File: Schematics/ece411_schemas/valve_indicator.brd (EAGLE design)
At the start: 85.1 x 53.6 mm, 66 parts, among them IC1 STM32F042K6T6, T1 2N2222, T2 2N2222, T3 2N2222, T4 2N2222, U1 DIODES_INC._AZ34063UMTR-G1DIO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, U2 DIODES_INC._AZ34063UMTR-G1DIO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

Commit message: added bypass caps, updated bom
needed to add 10uF ceramic in parallel with 100uF electro caps to decrease resistance to ground
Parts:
- added C0_H, C0_L: 10uF, rcl:C1206
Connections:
- net GND: now also C0_H.2, C0_L.2
- net N$1: now also C0_H.1, C0_L.1
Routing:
- net N$1: track 56.5 -> 65.0 mm
- net N$21: track 49.5 -> 51.5 mm
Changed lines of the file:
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@@
 <attribute name="MOUSER_PART_NUMBER" value="621-AZ34063UMTR-G1" x="-13.335" y="38.1" size="1.778" layer="27" rot="R180" display="off"/>
 <attribute name="MPN" value="AZ34063UMTR-G1" x="-13.335" y="38.1" size="1.778" layer="27" rot="R180" display="off"/>
-<attribute name="NAME" x="34.995" y="31.515" size="1" layer="25" rot="R180"/>
+<attribute name="NAME" x="35.63" y="37.865" size="0.8128" layer="25" rot="R180"/>
 <attribute name="NOMINAL_SUPPLY_CURRENT" value="4mA" x="-13.335" y="38.1" size="1.778" layer="27" rot="R180" display="off"/>
 <attribute name="NUMBER_OF_OUTPUTS" value="1" x="-13.335" y="38.1" size="1.778" layer="27" rot="R180" display="off"/>
@@
 <attribute name="MOUSER_PART_NUMBER" value="621-AZ34063UMTR-G1" x="51.435" y="22.86" size="1.778" layer="27" display="off"/>
 <attribute name="MPN" value="AZ34063UMTR-G1" x="51.435" y="22.86" size="1.778" layer="27" display="off"/>
-<attribute name="NAME" x="33.585" y="43.415" size="1" layer="25"/>
+<attribute name="NAME" x="34.22" y="43.415" size="0.8128" layer="25"/>
 <attribute name="NOMINAL_SUPPLY_CURRENT" value="4mA" x="51.435" y="22.86" size="1.778" layer="27" display="off"/>
 <attribute name="NUMBER_OF_OUTPUTS" value="1" x="51.435" y="22.86" size="1.778" layer="27" display="off"/>
@@
 <attribute name="POPULARITY" value="0" x="40.005" y="45.085" size="1.778" layer="27" rot="R180" display="off"/>
 <attribute name="SPICEPREFIX" value="C" x="40.005" y="45.085" size="1.778" layer="27" rot="R180" display="off"/>
+</element>
+<element name="C0_L" library="rcl" library_urn="urn:adsk.eagle:library:334" package="C1206" package3d_urn="urn:adsk.eagle:package:23618/2" value="10uF" x="34.29" y="45.72" smashed="yes" rot="R180">
+<attribute name="NAME" x="33.02" y="46.99" size="0.8128" layer="25"/>
+<attribute name="POPULARITY" value="24" x="34.29" y="45.72" size="1.778" layer="27" rot="R180" display="off"/>
+<attribute name="SPICEPREFIX" value="C" x="34.29" y="45.72" size="1.778" layer="27" rot="R180" display="off"/>
+</element>
+<element name="C0_H" library="rcl" library_urn="urn:adsk.eagle:library:334" package="C1206" package3d_urn="urn:adsk.eagle:package:23618/2" value="10uF" x="28.575" y="36.83" smashed="yes" rot="R90">
+<attribute name="NAME" x="29.845" y="38.1" size="0.8128" layer="25" rot="R270"/>
+<attribute name="POPULARITY" value="24" x="28.575" y="36.83" size="1.778" layer="27" rot="R90" display="off"/>
+<attribute name="SPICEPREFIX" value="C" x="28.575" y="36.83" size="1.778" layer="27" rot="R90" display="off"/>
 </element>
 </elements>
@@
 <via x="14.605" y="45.085" extent="1-16" drill="0.35"/>
 <via x="20.955" y="45.085" extent="1-16" drill="0.35"/>
-<via x="36.195" y="46.355" extent="1-16" drill="0.35"/>
+<via x="36.195" y="43.815" extent="1-16" drill="0.35"/>
 <via x="47.625" y="46.355" extent="1-16" drill="0.35"/>
 <via x="62.865" y="29.845" extent="1-16" drill="0.35"/>
@@
 <via x="3.81" y="31.75" extent="1-16" drill="0.35"/>
 <via x="3.81" y="38.735" extent="1-16" drill="0.35"/>
+<contactref element="C0_H" pad="2"/>
+<contactref element="C0_L" pad="2"/>
 </signal>
 <signal name="N$6">
@@
 <signal name="N$4">
 <contactref element="U1" pad="5"/>
-<wire x1="32.427" y1="36.195" x2="27.94" y2="36.195" width="0.3048" layer="1"/>
+<wire x1="32.427" y1="36.195" x2="30.48" y2="36.195" width="0.3048" layer="1"/>
 <contactref element="R1_L" pad="1"/>
 <contactref element="R2_L" pad="2"/>
-<wire x1="27.09" y1="37.045" x2="24.765" y2="37.045" width="0.3048" layer="1"/>
-<wire x1="27.94" y1="36.195" x2="27.09" y2="37.045" width="0.3048" layer="1"/>
+<wire x1="29.63" y1="37.045" x2="24.765" y2="37.045" width="0.3048" layer="1"/>
+<wire x1="30.48" y1="36.195" x2="29.63" y2="37.045" width="0.3048" layer="1"/>
 <wire x1="24.765" y1="37.045" x2="24.765" y2="39.155" width="0.3048" layer="1"/>
 </signal>
@@
 <wire x1="68.89" y1="36.52" x2="65.715" y2="39.695" width="0.3048" layer="1"/>
 <wire x1="56.825" y1="39.695" x2="65.715" y2="39.695" width="0.3048" layer="1"/>
-<wire x1="30.48" y1="41.91" x2="30.48" y2="43.307" width="0.3048" layer="1"/>
-<wire x1="30.48" y1="43.307" x2="34.2265" y2="47.0535" width="0.3048" layer="1"/>
+<wire x1="30.48" y1="41.91" x2="30.48" y2="45.847" width="0.3048" layer="1"/>
+<wire x1="30.48" y1="45.847" x2="32.3215" y2="47.6885" width="0.3048" layer="1"/>
 <wire x1="51.435" y1="44.45" x2="52.07" y2="44.45" width="0.3048" layer="1"/>
 <wire x1="52.07" y1="44.45" x2="56.825" y2="39.695" width="0.3048" layer="1"/>
-<wire x1="48.8315" y1="47.0535" x2="51.435" y2="44.45" width="0.3048" layer="1"/>
-<wire x1="34.2265" y1="47.0535" x2="48.8315" y2="47.0535" width="0.3048" layer="1"/>
+<wire x1="48.1965" y1="47.6885" x2="51.435" y2="44.45" width="0.3048" layer="1"/>
+<wire x1="32.3215" y1="47.6885" x2="48.1965" y2="47.6885" width="0.3048" layer="1"/>
 </signal>
 <signal name="+3V3">
@@
 <wire x1="33.655" y1="34.925" x2="34.29" y2="35.56" width="0.6096" layer="1"/>
 <wire x1="34.29" y1="35.56" x2="34.29" y2="37.465" width="0.6096" layer="1"/>
-<wire x1="24.172" y1="33.655" x2="29.845" y2="33.655" width="0.6096" layer="1"/>
+<wire x1="24.172" y1="33.655" x2="28.575" y2="33.655" width="0.6096" layer="1"/>
 <contactref element="RS_L" pad="1"/>
+<wire x1="28.575" y1="33.655" x2="29.845" y2="33.655" width="0.6096" layer="1"/>
 <wire x1="32.385" y1="29.845" x2="35.98" y2="29.845" width="0.6096" layer="1"/>
 <contactref element="C1_L" pad="1"/>
@@
 <wire x1="41.275" y1="45.085" x2="41.49" y2="44.87" width="0.6096" layer="1"/>
 <wire x1="41.49" y1="44.87" x2="41.49" y2="41.91" width="0.6096" layer="1"/>
+<contactref element="C0_H" pad="1"/>
+<contactref element="C0_L" pad="1"/>
+<wire x1="28.575" y1="35.43" x2="28.575" y2="33.655" width="0.6096" layer="1"/>
+<wire x1="35.69" y1="45.72" x2="37.465" y2="45.72" width="0.6096" layer="1"/>
+<wire x1="37.465" y1="45.72" x2="38.1" y2="46.355" width="0.6096" layer="1"/>
+<wire x1="38.1" y1="46.355" x2="40.64" y2="46.355" width="0.6096" layer="1"/>
+<wire x1="40.64" y1="46.355" x2="41.275" y2="45.72" width="0.6096" layer="1"/>
+<wire x1="41.275" y1="45.72" x2="41.275" y2="45.085" width="0.6096" layer="1"/>
 </signal>
 <signal name="N$39">

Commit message: updates to board, added libraries
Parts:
- removed JTAG_EMUL: JTAG_EMUL, pinhead:1X05
- added BATT_BACKUP: (no value), SparkFun-Connectors:JST-2-SMD
- added D3: SB240, diode:DO41-7.6
- added J1: 1.27MM-SWD-CONNECTOR, J-CNC-3220-10-0100-00-ARM-SWD-port:1.27MM_2X5
- moved D2 1.27 mm to (73.7, 33.7)
- moved D1 0.90 mm to (59.1, 37.5)
- moved L2 0.64 mm to (50.8, 41.9)
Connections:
- new net N$16: BATT_BACKUP.2, D3.A
- net GND: now also BATT_BACKUP.1; no longer JTAG_EMUL.2
- net N$1: now also D3.C
- net N$30: now also J1.SWDIO; no longer JTAG_EMUL.3
- net N$31: now also J1.SWDCLK; no longer JTAG_EMUL.4
- net N$9: no longer JTAG_EMUL.5
- net VCC: no longer JTAG_EMUL.1
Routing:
- net VCC: track 230.4 -> 225.5 mm
- net N$9: track 29.1 -> 26.6 mm
- net N$30: track 43.2 -> 40.6 mm
- net N$31: track 43.1 -> 41.2 mm
- net N$21: track 51.5 -> 52.8 mm
- net N$5: track 21.9 -> 21.0 mm
- net GND: track 53.2 -> 52.3 mm

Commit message: updated board
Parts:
- removed BATT_BACKUP: (no value), SparkFun-Connectors:JST-2-SMD
- removed IC1: STM32F042K6T6, SamacSys_Parts:QFP80P900X900X160-32N
- added BATT: LED1, pinhead:1X02
- added C10, C11, C12: 100nF, rcl:C0603
- added U3: STM32F042K6, U-ST-STM32F042K-uC:QFP32-7X7
- R1_L: value 4.7k -> 3.6k
- R2_L: value 2.5k -> 2.2k
- moved J1 40.9 mm to (24.8, 27.3), turned to 90 degrees
- moved SD_CARD 8.26 mm to (59.1, 44.5)
- moved T1 6.02 mm to (70.5, 24.1)
- moved R13 5.99 mm to (76.2, 21.0), turned to 0 degrees
- moved T4 5.43 mm to (74.3, 24.8), turned to 180 degrees
- moved R11 5.12 mm to (79.4, 27.3), turned to 180 degrees
- moved L2 4.44 mm to (50.8, 37.5)
- moved R10 3.42 mm to (71.1, 21.0), turned to 180 degrees
- moved T2 2.84 mm to (79.4, 22.9), turned to 180 degrees
- moved R12 1.42 mm to (77.5, 30.5)
- moved T3 1.42 mm to (73.7, 30.5)
- turned BUZZER to 0 degrees
- turned LED1 to 0 degrees
- turned LED2 to 0 degrees
- turned LED3 to 0 degrees
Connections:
- removed net N$23: IC1.21, T2.B
- removed net N$39: R13.2, T4.C
- removed net N$40: R12.2, T3.C
- removed net N$41: R11.2, T2.C
- removed net N$42: R10.2, T1.C
- removed net VCC: C3_L.1, HES1.1, HES2.1, HES3.1, HES4.1, HES5.1, HES6.1, HES7.1, HES8.1, HES9.1, IC1.1, IC1.17, IC1.5, L1.2, R1.1, R1_L.2, R2.1, R3.1, R4.1, R5.1, R6.1, R7.1, R8.1, R9.1, SD_CARD.2
- new net +12V: BUZZER.1, C3_H.1, HES1.1, HES2.1, HES3.1, HES4.1, HES5.1, HES6.1, HES7.1, HES8.1, HES9.1, L2.2, LED1.1, LED2.1, LED3.1, R1.1, R1_H.2, R2.1, R3.1, R4.1, R5.1, R6.1, R7.1, R8.1, R9.1
- new net N$10: LED1.2, T1.C
- new net N$32: J1.!RESET, U3.4
- new net N$33: LED3.2, T3.C
- new net N$34: T4.B, U3.6
- new net N$35: T2.B, U3.21
- net +3V3: now also C10.1, C11.1, C12.1, C3_L.1, J1.VTREF, L1.2, R1_L.2, SD_CARD.2, U3.1, U3.17, U3.5; no longer C3_H.1, L2.2, R10.1, R11.1, R12.1, R13.1, R1_H.2
- net GND: now also BATT.2, C10.2, C11.2, C12.2, J1.GND, J1.GND@2, J1.GNDDET, R10.2, R11.2, R12.2, R13.2, U3.16, U3.32; no longer BATT_BACKUP.1, BUZZER.2, IC1.16, IC1.32, LED1.2, LED2.2, LED3.2
- net N$11: now also U3.11; no longer IC1.11
- net N$12: now also U3.12; no longer IC1.12
- net N$13: now also U3.13; no longer IC1.13
- net N$14: now also U3.18; no longer IC1.18
- net N$15: now also U3.19; no longer IC1.19
- net N$16: now also BATT.1; no longer BATT_BACKUP.2
- net N$17: now also U3.10; no longer IC1.10
- net N$22: now also U3.20; no longer IC1.20
- net N$24: now also U3.22; no longer IC1.22
- net N$25: now also LED2.2, T2.C; no longer IC1.6, T4.B
- net N$26: now also R10.1; no longer LED1.1
- net N$27: now also R11.1; no longer LED2.1
- net N$28: now also BUZZER.2, T4.C; no longer LED3.1, T3.E
- net N$29: now also R13.1; no longer BUZZER.1
- net N$30: now also U3.23; no longer IC1.23
- net N$31: now also R12.1, T3.E; no longer IC1.24, J1.SWDCLK
- net N$6: now also U3.7; no longer IC1.7
- net N$7: now also U3.8; no longer IC1.8
- net N$8: now also U3.9; no longer IC1.9
- net N$9: now also J1.SWDCLK, U3.24; no longer IC1.4
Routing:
- net +12V: track 0.00 -> 261.1 mm, vias 0 -> 11
- net VCC: track 225.5 -> 0.00 mm, vias 10 -> 0
- net N$31: track 41.2 -> 3.11 mm, vias 1 -> 0
- net N$1: track 65.0 -> 98.1 mm
- net N$32: track 0.00 -> 31.7 mm, vias 0 -> 1
- net +3V3: track 78.4 -> 108.0 mm, vias 4 -> 2
- net N$33: track 0.00 -> 21.8 mm, vias 0 -> 2
- net N$10: track 0.00 -> 21.8 mm
- net N$9: track 26.6 -> 44.8 mm
- net N$23: track 18.1 -> 0.00 mm
- net N$34: track 0.00 -> 17.8 mm, vias 0 -> 2
- net N$35: track 0.00 -> 16.5 mm
- net N$28: track 26.4 -> 11.8 mm, vias 1 -> 0
- net N$27: track 17.9 -> 3.39 mm
- net N$26: track 15.2 -> 2.38 mm
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
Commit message: bom, layout, attribute, device
added attributes to rest of parts
made power lines thicker for dissapation
editted az34.. device to remedy errors
added test points
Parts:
- removed J1: 1.27MM-SWD-CONNECTOR, J-CNC-3220-10-0100-00-ARM-SWD-port:1.27MM_2X5
- added CM1: FTSH-105-XX-X-DV-K, J-Samtec-FTSH-105-XXX-DV-K-ARM-SWD:CON10_2X5_DUK_FTSH
- added TP10V, TP3V3, TP3V3J, TPJGND, TPNRST, TPOE, TPSCLK, TPSIO: TEST-POINT-LARGE-SQUARE, oresat-misc:1X01
- D1, D2: value ON_SEMICONDUCTOR_1N5819GON_SEMICONDUCTOR_1N5819G_0_0 -> 1N5819G_0_0
- U1, U2: value DIODES_INC._AZ34063UMTR-G1DIODES_INC._AZ34063UMTR-G1_0_0 -> AZ34063UMTR-G1
- moved R2_H 7.62 mm to (44.5, 46.4), turned to 0 degrees
- moved R12 0.90 mm to (78.1, 31.1), turned to 0 degrees
- moved C10 0.90 mm to (54.0, 34.3)
- moved D1 0.64 mm to (59.1, 36.8)
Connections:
- removed net +12V: BUZZER.1, C3_H.1, HES1.1, HES2.1, HES3.1, HES4.1, HES5.1, HES6.1, HES7.1, HES8.1, HES9.1, L2.2, LED1.1, LED2.1, LED3.1, R1.1, R1_H.2, R2.1, R3.1, R4.1, R5.1, R6.1, R7.1, R8.1, R9.1
- removed net N$1: C0_H.1, C0_L.1, C1_H.1, C1_L.1, D3.C, POE_IN.PWR1, RS_H.1, RS_L.1, U1.6, U2.6
- new net +10V: BUZZER.1, C3_H.1, HES1.1, HES2.1, HES3.1, HES4.1, HES5.1, HES6.1, HES7.1, HES8.1, HES9.1, L2.2, LED1.1, LED2.1, LED3.1, R1.1, R1_H.2, R2.1, R3.1, R4.1, R5.1, R6.1, R7.1, R8.1, R9.1, TP10V.1
- new net POE: C0_H.1, C0_L.1, C1_H.1, C1_L.1, D3.C, POE_IN.PWR1, RS_H.1, RS_L.1, TPOE.1, U1.6, U2.6
- net +3V3: now also CM1.1, TP3V3.1, TP3V3J.1; no longer J1.VTREF
- net GND: now also CM1.3, CM1.5, CM1.9, TPJGND.1; no longer J1.GND, J1.GND@2, J1.GNDDET
- net N$30: now also CM1.2, TPSIO.1; no longer J1.SWDIO
- net N$32: now also CM1.10, TPNRST.1; no longer J1.!RESET
- net N$9: now also CM1.4, TPSCLK.1; no longer J1.SWDCLK
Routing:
- net +10V: track 0.00 -> 261.4 mm, vias 0 -> 11
- net +12V: track 261.1 -> 0.00 mm, vias 11 -> 0
- net POE: track 0.00 -> 103.3 mm
- net N$1: track 98.1 -> 0.00 mm
- net N$20: track 8.72 -> 19.0 mm
- net +3V3: track 108.0 -> 116.2 mm, vias 2 -> 3
- net N$9: track 44.8 -> 50.9 mm, vias 1 -> 2
- net N$30: track 45.7 -> 50.1 mm, vias 1 -> 2
- net GND: track 42.8 -> 40.5 mm, vias 50 -> 83
- net N$32: vias 1 -> 2

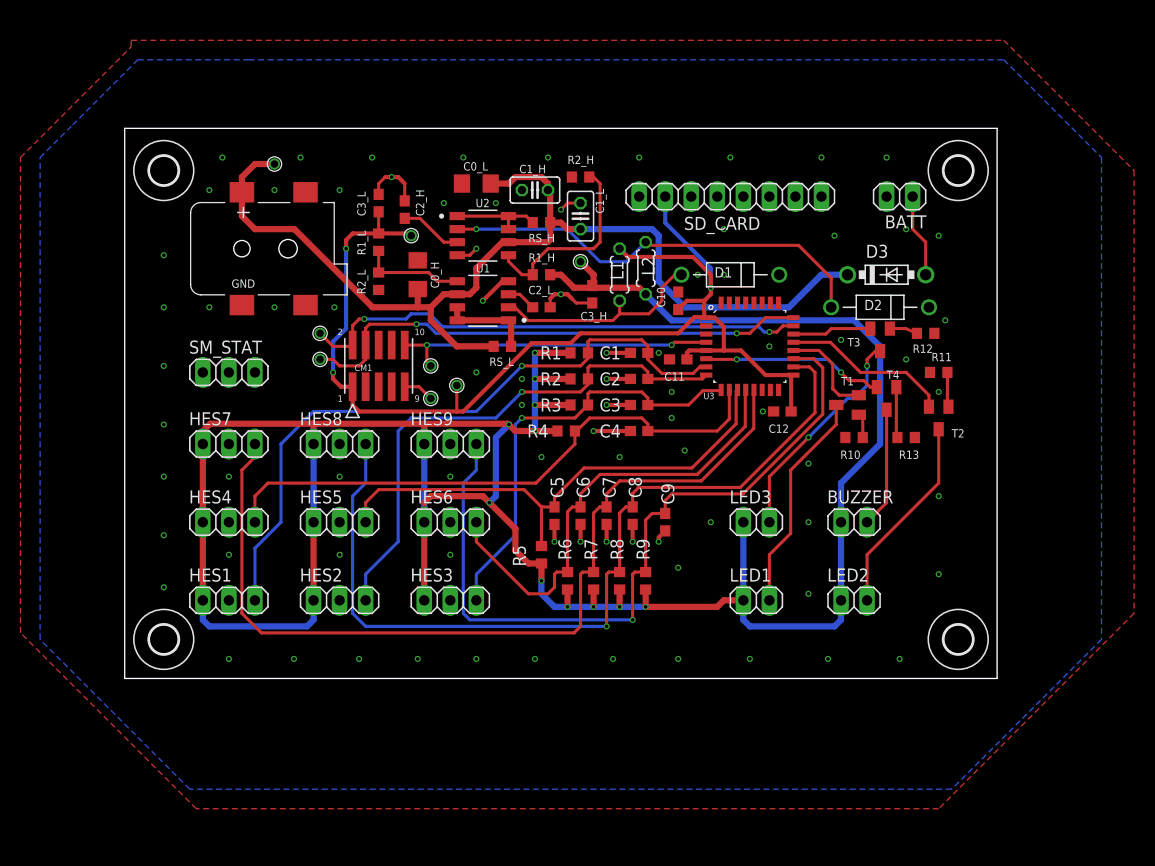
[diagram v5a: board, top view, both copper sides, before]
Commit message: added state machine uart conn, labels
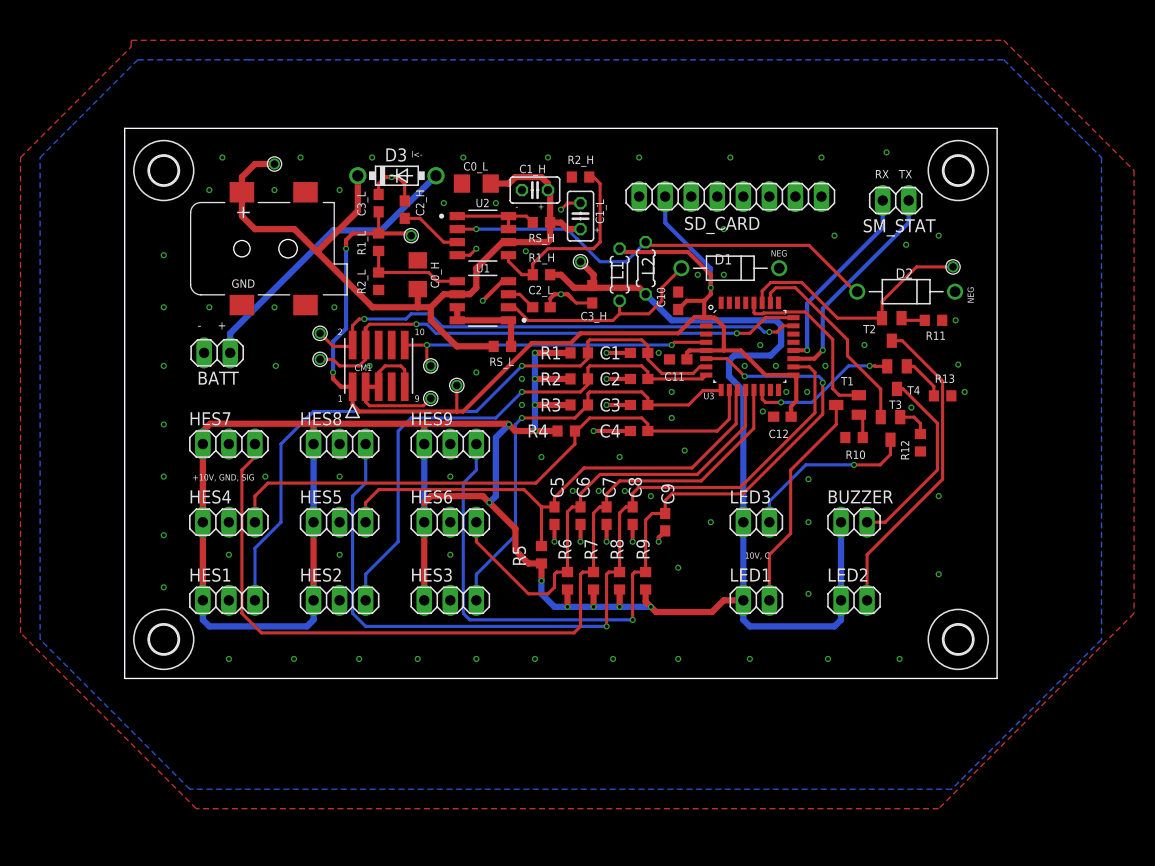
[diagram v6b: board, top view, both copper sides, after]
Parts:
- added TPBASE: TEST-POINT-LARGE-SQUARE, oresat-misc:1X01
- SM_STAT: device pinhead:1X03 -> pinhead:1X02
- moved BATT 68.3 mm to (9.02, 29.2)
- moved SM_STAT 67.2 mm to (75.2, 44.1), turned to 180 degrees
- moved D3 48.7 mm to (26.5, 46.5)
- moved R12 10.7 mm to (77.6, 20.4), turned to 270 degrees
- moved T2 9.77 mm to (74.8, 31.5)
- moved T3 8.70 mm to (74.7, 21.8)
- moved R13 5.40 mm to (79.8, 25.0)
- moved R11 5.11 mm to (78.9, 32.4), turned to 0 degrees
- moved D2 2.96 mm to (76.2, 35.2)
- moved T4 2.27 mm to (75.3, 26.8)
- moved D1 0.64 mm to (59.1, 37.5)
- moved C12 0.51 mm to (64.1, 23.0)
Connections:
- new net N$23: CM1.3, CM1.5, CM1.9, TPJGND.1
- new net UART-RX: SM_STAT.2, U3.20
- new net UART-TX: SM_STAT.1, U3.19
- net GND: no longer CM1.3, CM1.5, CM1.9, SM_STAT.2, TPJGND.1
- net N$15: now also U3.6; no longer U3.19
- net N$22: now also U3.28; no longer U3.20
- net N$24: now also U3.26; no longer U3.22
- net N$34: now also U3.14; no longer U3.6
- net N$35: now also TPBASE.1, U3.27; no longer U3.21
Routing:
- net POE: track 103.3 -> 79.3 mm
- net UART-TX: track 0.00 -> 21.3 mm, vias 0 -> 1
- net N$16: track 8.15 -> 28.3 mm
- net UART-RX: track 0.00 -> 19.0 mm, vias 0 -> 1
- net N$23: track 0.00 -> 15.6 mm
- net N$24: track 7.72 -> 19.7 mm
- net N$25: track 19.6 -> 31.0 mm
- net N$35: track 16.5 -> 24.6 mm
- net N$22: track 9.59 -> 17.5 mm
- net N$15: track 74.7 -> 82.5 mm, vias 1 -> 3
- net N$28: track 11.8 -> 18.9 mm
- net +10V: track 261.4 -> 256.8 mm
- net N$33: track 21.8 -> 17.2 mm, vias 2 -> 1
- net N$34: track 17.8 -> 14.7 mm
- net GND: track 40.5 -> 37.5 mm, vias 83 -> 96
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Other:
- board text added: "+ -"
- board text added: "+10V, GND, SIG"
- board text added: "- +"
- board text added: "10V, C"
- board text added: "NEG"
- board text added: "RX TX"
- board text added: "l<-"
